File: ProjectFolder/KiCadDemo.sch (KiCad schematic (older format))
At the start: 9 parts, among them J1 1992, J2 TSW-103-07-T-S, J3 TSW-103-07-T-S, J4 TSW-103-07-T-S, J5 TSW-103-07-T-S

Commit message: Mostly finished PCB layout
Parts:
- added J6, J7: TSW-103-07-T-S, tsw-103-07-t-s:tsw-103-07-t-s, symbol TSW-103-07-T-S
- C2, C3: footprint Capacitors_SMD:C_1206 -> Capacitors_SMD:C_0805
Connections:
- net A1: now also J6.1, J7.1
- net A2: now also J6.2, J7.2
- net A3: now also J6.3, J7.3
- net AA: now also J1.26; no longer J1.32
- net AB: now also J1.33; no longer J1.36
- net CA: now also J1.35; no longer J1.38
- net CB: now also J1.38; no longer J1.40
- net S1C1: now also J3.1; no longer J2.1
- net S1C2: now also J3.2; no longer J2.2
- net S1C3: now also J3.3; no longer J2.3
- net S1_EN: now also J1.36; no longer J1.33
- net S2C1: now also J2.1; no longer J3.1
- net S2C2: now also J2.2; no longer J3.2
- net S2C3: now also J2.3; no longer J3.3
- net S2_EN: now also J1.40; no longer J1.35
- net S3_EN: now also J1.32; no longer J1.26
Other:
- moved on the sheet: J2, J3, J4, J5
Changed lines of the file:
@@
 L TSW-103-07-T-S J2
 U 1 1 55078EDE
-P 9200 3250
-F 0 "J2" H 9200 3500 60  0000 L CNN
-F 1 "TSW-103-07-T-S" H 9200 3000 60  0000 L CNN
-F 2 "tsw-103-07-t-s:tsw-103-07-t-s" H 9250 3250 60  0001 C CNN
-F 3 "" H 9250 3250 60  0000 C CNN
-F 4 "Samtec" H 9200 3250 60  0001 C CNN "Manufacturer"
-F 5 "TSW-103-07-T-S" H 9200 3250 60  0001 C CNN "Manufacturer Part Number"
-F 6 "Digi-Key" H 9200 3250 60  0001 C CNN "Supplier"
-F 7 "SAM1035-03-ND" H 9200 3250 60  0001 C CNN "Supplier Part Number"
-	1    9200 3250
-	1    0    0    -1
-$EndComp
-Text Label 8650 3150 0    60   ~ 0
+P 8250 3700
+F 0 "J2" H 8250 3950 60  0000 L CNN
+F 1 "TSW-103-07-T-S" H 8250 3450 60  0000 L CNN
+F 2 "tsw-103-07-t-s:tsw-103-07-t-s" H 8300 3700 60  0001 C CNN
+F 3 "" H 8300 3700 60  0000 C CNN
+F 4 "Samtec" H 8250 3700 60  0001 C CNN "Manufacturer"
+F 5 "TSW-103-07-T-S" H 8250 3700 60  0001 C CNN "Manufacturer Part Number"
+F 6 "Digi-Key" H 8250 3700 60  0001 C CNN "Supplier"
+F 7 "SAM1035-03-ND" H 8250 3700 60  0001 C CNN "Supplier Part Number"
+	1    8250 3700
+	1    0    0    -1
+$EndComp
+Text Label 7700 4350 0    60   ~ 0
 S1C1
 Wire Wire Line
-	8650 3150 9000 3150
-Text Label 8650 3250 0    60   ~ 0
+	7700 4350 8050 4350
+Text Label 7700 4450 0    60   ~ 0
 S1C2
 Wire Wire Line
-	8650 3250 9000 3250
-Text Label 8650 3350 0    60   ~ 0
+	7700 4450 8050 4450
+Text Label 7700 4550 0    60   ~ 0
 S1C3
 Wire Wire Line
-	8650 3350 9000 3350
-Text Label 8650 3900 0    60   ~ 0
+	7700 4550 8050 4550
+Text Label 7700 3600 0    60   ~ 0
 S2C1
 Wire Wire Line
-	8650 3900 9000 3900
-Text Label 8650 4000 0    60   ~ 0
+	7700 3600 8050 3600
+Text Label 7700 3700 0    60   ~ 0
 S2C2
 Wire Wire Line
-	8650 4000 9000 4000
-Text Label 8650 4100 0    60   ~ 0
+	7700 3700 8050 3700
+Text Label 7700 3800 0    60   ~ 0
 S2C3
 Wire Wire Line
-	8650 4100 9000 4100
-Text Label 8650 4650 0    60   ~ 0
+	7700 3800 8050 3800
+Text Label 7700 5100 0    60   ~ 0
 S3C1
 Wire Wire Line
-	8650 4650 9000 4650
-Text Label 8650 4750 0    60   ~ 0
+	7700 5100 8050 5100
+Text Label 7700 5200 0    60   ~ 0
 S3C2
 Wire Wire Line
-	8650 4750 9000 4750
-Text Label 8650 4850 0    60   ~ 0
+	7700 5200 8050 5200
+Text Label 7700 5300 0    60   ~ 0
 S3C3
 Wire Wire Line
-	8650 4850 9000 4850
-Text Label 8650 5400 0    60   ~ 0
+	7700 5300 8050 5300
+Text Label 9450 3600 0    60   ~ 0
 A1
 Wire Wire Line
-	8650 5400 9000 5400
-Text Label 8650 5500 0    60   ~ 0
+	9450 3600 9800 3600
+Text Label 9450 3700 0    60   ~ 0
 A2
 Wire Wire Line
-	8650 5500 9000 5500
-Text Label 8650 5600 0    60   ~ 0
+	9450 3700 9800 3700
+Text Label 9450 3800 0    60   ~ 0
 A3
 Wire Wire Line
-	8650 5600 9000 5600
+	9450 3800 9800 3800
+Text Label 2700 5150 2    60   ~ 0
+S2_EN
 Text Label 950  4950 0    60   ~ 0
-S2_EN
+CA
 Text Label 2700 5050 2    60   ~ 0
-CA
-Text Label 2700 5150 2    60   ~ 0
 CB
+Text Label 2700 4750 2    60   ~ 0
+S3_EN
 Text Label 2700 4450 2    60   ~ 0
-S3_EN
-Text Label 2700 4750 2    60   ~ 0
 AA
+Text Label 950  4850 0    60   ~ 0
+AB
 Text Label 2700 4950 2    60   ~ 0
-AB
-Text Label 950  4850 0    60   ~ 0
 S1_EN
 Wire Wire Line
@@
 F 0 "C2" H 2350 6500 50  0000 L CNN
 F 1 "0.1u" H 2350 6300 50  0000 L CNN
-F 2 "Capacitors_SMD:C_1206" H 2338 6250 30  0001 C CNN
+F 2 "Capacitors_SMD:C_0805" H 2338 6250 30  0001 C CNN
 F 3 "" H 2300 6400 60  0000 C CNN
 F 4 "16V" H 2450 6200 60  0001 C CNN "Voltage"
@@
 F 0 "C3" H 2800 6500 50  0000 L CNN
 F 1 "10u" H 2800 6300 50  0000 L CNN
-F 2 "Capacitors_SMD:C_1206" H 2788 6250 30  0001 C CNN
+F 2 "Capacitors_SMD:C_0805" H 2788 6250 30  0001 C CNN
 F 3 "" H 2750 6400 60  0000 C CNN
 F 4 "16V" H 2900 6200 60  0001 C CNN "Voltage"
@@
 L TSW-103-07-T-S J3
 U 1 1 550C2E47
-P 9200 4000
-F 0 "J3" H 9200 4250 60  0000 L CNN
-F 1 "TSW-103-07-T-S" H 9200 3750 60  0000 L CNN
-F 2 "tsw-103-07-t-s:tsw-103-07-t-s" H 9250 4000 60  0001 C CNN
-F 3 "" H 9250 4000 60  0000 C CNN
-F 4 "Samtec" H 9200 4000 60  0001 C CNN "Manufacturer"
-F 5 "TSW-103-07-T-S" H 9200 4000 60  0001 C CNN "Manufacturer Part Number"
-F 6 "Digi-Key" H 9200 4000 60  0001 C CNN "Supplier"
-F 7 "SAM1035-03-ND" H 9200 4000 60  0001 C CNN "Supplier Part Number"
-	1    9200 4000
+P 8250 4450
+F 0 "J3" H 8250 4700 60  0000 L CNN
+F 1 "TSW-103-07-T-S" H 8250 4200 60  0000 L CNN
+F 2 "tsw-103-07-t-s:tsw-103-07-t-s" H 8300 4450 60  0001 C CNN
+F 3 "" H 8300 4450 60  0000 C CNN
+F 4 "Samtec" H 8250 4450 60  0001 C CNN "Manufacturer"
+F 5 "TSW-103-07-T-S" H 8250 4450 60  0001 C CNN "Manufacturer Part Number"
+F 6 "Digi-Key" H 8250 4450 60  0001 C CNN "Supplier"
+F 7 "SAM1035-03-ND" H 8250 4450 60  0001 C CNN "Supplier Part Number"
+	1    8250 4450
 	1    0    0    -1
 $EndComp
@@
 L TSW-103-07-T-S J4
 U 1 1 550C2E90
-P 9200 4750
-F 0 "J4" H 9200 5000 60  0000 L CNN
-F 1 "TSW-103-07-T-S" H 9200 4500 60  0000 L CNN
-F 2 "tsw-103-07-t-s:tsw-103-07-t-s" H 9250 4750 60  0001 C CNN
-F 3 "" H 9250 4750 60  0000 C CNN
-F 4 "Samtec" H 9200 4750 60  0001 C CNN "Manufacturer"
-F 5 "TSW-103-07-T-S" H 9200 4750 60  0001 C CNN "Manufacturer Part Number"
-F 6 "Digi-Key" H 9200 4750 60  0001 C CNN "Supplier"
-F 7 "SAM1035-03-ND" H 9200 4750 60  0001 C CNN "Supplier Part Number"
-	1    9200 4750
+P 8250 5200
+F 0 "J4" H 8250 5450 60  0000 L CNN
+F 1 "TSW-103-07-T-S" H 8250 4950 60  0000 L CNN
+F 2 "tsw-103-07-t-s:tsw-103-07-t-s" H 8300 5200 60  0001 C CNN
+F 3 "" H 8300 5200 60  0000 C CNN
+F 4 "Samtec" H 8250 5200 60  0001 C CNN "Manufacturer"
+F 5 "TSW-103-07-T-S" H 8250 5200 60  0001 C CNN "Manufacturer Part Number"
+F 6 "Digi-Key" H 8250 5200 60  0001 C CNN "Supplier"
+F 7 "SAM1035-03-ND" H 8250 5200 60  0001 C CNN "Supplier Part Number"
+	1    8250 5200
 	1    0    0    -1
 $EndComp
@@
 L TSW-103-07-T-S J5
 U 1 1 550C2EDC
-P 9200 5500
-F 0 "J5" H 9200 5750 60  0000 L CNN
-F 1 "TSW-103-07-T-S" H 9200 5250 60  0000 L CNN
-F 2 "tsw-103-07-t-s:tsw-103-07-t-s" H 9250 5500 60  0001 C CNN
-F 3 "" H 9250 5500 60  0000 C CNN
-F 4 "Samtec" H 9200 5500 60  0001 C CNN "Manufacturer"
-F 5 "TSW-103-07-T-S" H 9200 5500 60  0001 C CNN "Manufacturer Part Number"
-F 6 "Digi-Key" H 9200 5500 60  0001 C CNN "Supplier"
-F 7 "SAM1035-03-ND" H 9200 5500 60  0001 C CNN "Supplier Part Number"
-	1    9200 5500
-	1    0    0    -1
-$EndComp
+P 10000 3700
+F 0 "J5" H 10000 3950 60  0000 L CNN
+F 1 "TSW-103-07-T-S" H 9400 3450 60  0000 L CNN
+F 2 "tsw-103-07-t-s:tsw-103-07-t-s" H 10050 3700 60  0001 C CNN
+F 3 "" H 10050 3700 60  0000 C CNN
+F 4 "Samtec" H 10000 3700 60  0001 C CNN "Manufacturer"
+F 5 "TSW-103-07-T-S" H 10000 3700 60  0001 C CNN "Manufacturer Part Number"
+F 6 "Digi-Key" H 10000 3700 60  0001 C CNN "Supplier"
+F 7 "SAM1035-03-ND" H 10000 3700 60  0001 C CNN "Supplier Part Number"
+	1    10000 3700
+	1    0    0    -1
+$EndComp
+Text Label 9450 4350 0    60   ~ 0
+A1
+Wire Wire Line
+	9450 4350 9800 4350
+Text Label 9450 4450 0    60   ~ 0
+A2
+Wire Wire Line
+	9450 4450 9800 4450
+Text Label 9450 4550 0    60   ~ 0
+A3
+Wire Wire Line
+	9450 4550 9800 4550
+$Comp
+L TSW-103-07-T-S J6
+U 1 1 550A6C58
+P 10000 4450
+F 0 "J6" H 10000 4700 60  0000 L CNN
+F 1 "TSW-103-07-T-S" H 9350 4200 60  0000 L CNN
+F 2 "tsw-103-07-t-s:tsw-103-07-t-s" H 10050 4450 60  0001 C CNN
+F 3 "" H 10050 4450 60  0000 C CNN
+F 4 "Samtec" H 10000 4450 60  0001 C CNN "Manufacturer"
+F 5 "TSW-103-07-T-S" H 10000 4450 60  0001 C CNN "Manufacturer Part Number"
+F 6 "Digi-Key" H 10000 4450 60  0001 C CNN "Supplier"
+F 7 "SAM1035-03-ND" H 10000 4450 60  0001 C CNN "Supplier Part Number"
+	1    10000 4450
+	1    0    0    -1
+$EndComp
+Text Label 9450 5100 0    60   ~ 0
+A1
+Wire Wire Line
+	9450 5100 9800 5100
+Text Label 9450 5200 0    60   ~ 0
+A2
+Wire Wire Line
+	9450 5200 9800 5200
+Text Label 9450 5300 0    60   ~ 0
+A3
+Wire Wire Line
+	9450 5300 9800 5300
+$Comp
+L TSW-103-07-T-S J7
+U 1 1 550A939F
+P 10000 5200
+F 0 "J7" H 10000 5450 60  0000 L CNN
+F 1 "TSW-103-07-T-S" H 9350 4950 60  0000 L CNN
+F 2 "tsw-103-07-t-s:tsw-103-07-t-s" H 10050 5200 60  0001 C CNN
+F 3 "" H 10050 5200 60  0000 C CNN
+F 4 "Samtec" H 10000 5200 60  0001 C CNN "Manufacturer"
+F 5 "TSW-103-07-T-S" H 10000 5200 60  0001 C CNN "Manufacturer Part Number"
+F 6 "Digi-Key" H 10000 5200 60  0001 C CNN "Supplier"
+F 7 "SAM1035-03-ND" H 10000 5200 60  0001 C CNN "Supplier Part Number"
+	1    10000 5200
+	1    0    0    -1
+$EndComp

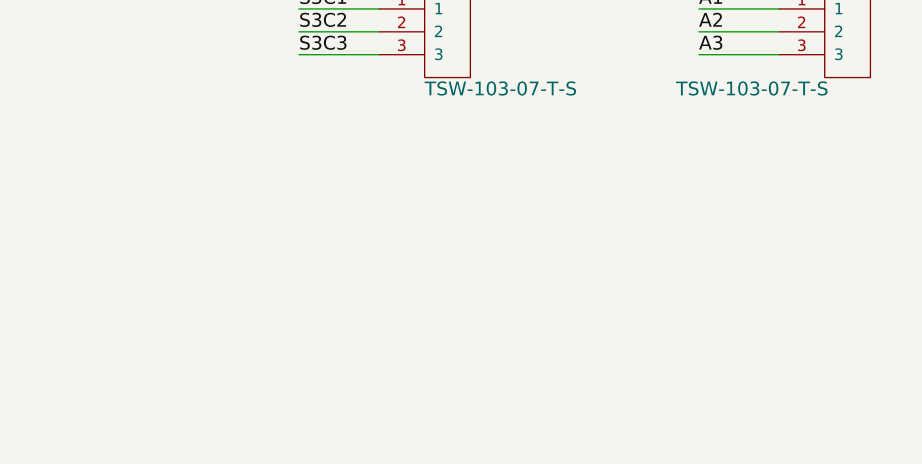
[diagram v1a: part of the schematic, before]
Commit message: Added mounting holes, fixed Raspberry Pi reference footprint mounting hole locations, and removed inaccurate mechanical drawing
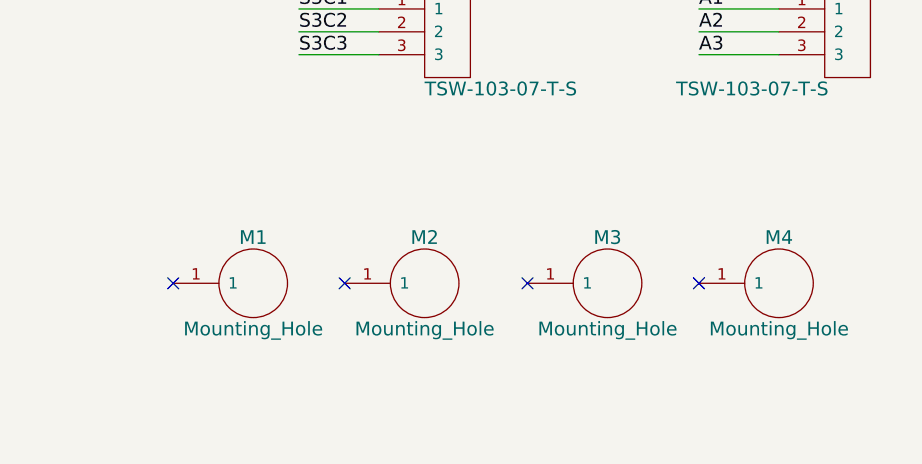
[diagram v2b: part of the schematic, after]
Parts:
- added M1, M2, M3, M4: Mounting_Hole, mounting_hole:mounting_hole_2.75mm_pth, symbol Mounting_Hole
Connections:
- no-connect marks 23 -> 27
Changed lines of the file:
@@
 LIBS:tsw-103-07-t-s
 LIBS:uln2003adr
+LIBS:mounting_hole
 LIBS:KiCadDemo-cache
 EELAYER 25 0
@@
 Sheet 1 2
 Title "Raspberry Pi 3x3x3 LED Cube Shield, Main PCB"
-Date "Tuesday, March 17, 2015"
+Date "Thursday, March 19, 2015"
 Rev "-"
 Comp ""
@@
 	1    0    0    -1
 $EndComp
+$Comp
+L Mounting_Hole M4
+U 1 1 550B8F13
+P 9800 6300
+F 0 "M4" H 9800 6500 60  0000 C CNN
+F 1 "Mounting_Hole" H 9800 6100 60  0000 C CNN
+F 2 "mounting_hole:mounting_hole_2.75mm_pth" H 9800 6300 60  0001 C CNN
+F 3 "" H 9800 6300 60  0000 C CNN
+	1    9800 6300
+	1    0    0    -1
+$EndComp
+$Comp
+L Mounting_Hole M3
+U 1 1 550B8ED3
+P 9050 6300
+F 0 "M3" H 9050 6500 60  0000 C CNN
+F 1 "Mounting_Hole" H 9050 6100 60  0000 C CNN
+F 2 "mounting_hole:mounting_hole_2.75mm_pth" H 9050 6300 60  0001 C CNN
+F 3 "" H 9050 6300 60  0000 C CNN
+	1    9050 6300
+	1    0    0    -1
+$EndComp
+$Comp
+L Mounting_Hole M2
+U 1 1 550B8E7F
+P 8250 6300
+F 0 "M2" H 8250 6500 60  0000 C CNN
+F 1 "Mounting_Hole" H 8250 6100 60  0000 C CNN
+F 2 "mounting_hole:mounting_hole_2.75mm_pth" H 8250 6300 60  0001 C CNN
+F 3 "" H 8250 6300 60  0000 C CNN
+	1    8250 6300
+	1    0    0    -1
+$EndComp
+$Comp
+L Mounting_Hole M1
+U 1 1 550B74AD
+P 7500 6300
+F 0 "M1" H 7500 6500 60  0000 C CNN
+F 1 "Mounting_Hole" H 7500 6100 60  0000 C CNN
+F 2 "mounting_hole:mounting_hole_2.75mm_pth" H 7500 6300 60  0001 C CNN
+F 3 "" H 7500 6300 60  0000 C CNN
+	1    7500 6300
+	1    0    0    -1
+$EndComp
+NoConn ~ 7150 6300
+NoConn ~ 7900 6300
+NoConn ~ 8700 6300
+NoConn ~ 9450 6300
 $EndSCHEMATC

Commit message: branch to store exercise project, remove mounting holes including libraries
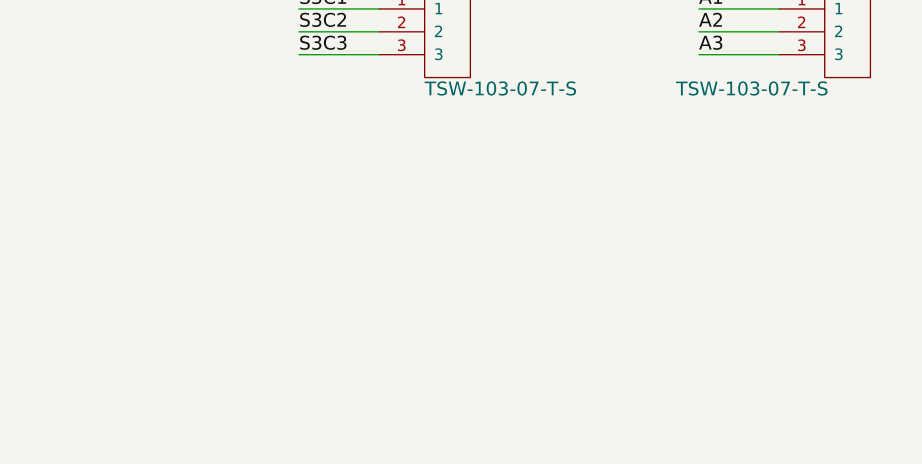
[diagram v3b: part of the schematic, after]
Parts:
- removed M1, M2, M3, M4: Mounting_Hole, mounting_hole:mounting_hole_2.75mm_pth, symbol Mounting_Hole
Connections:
- no-connect marks 27 -> 23
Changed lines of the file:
@@
 LIBS:tsw-103-07-t-s
 LIBS:uln2003adr
-LIBS:mounting_hole
 LIBS:KiCadDemo-cache
 EELAYER 25 0
@@
 	1    0    0    -1
 $EndComp
-$Comp
-L Mounting_Hole M4
-U 1 1 550B8F13
-P 9800 6300
-F 0 "M4" H 9800 6500 60  0000 C CNN
-F 1 "Mounting_Hole" H 9800 6100 60  0000 C CNN
-F 2 "mounting_hole:mounting_hole_2.75mm_pth" H 9800 6300 60  0001 C CNN
-F 3 "" H 9800 6300 60  0000 C CNN
-	1    9800 6300
-	1    0    0    -1
-$EndComp
-$Comp
-L Mounting_Hole M3
-U 1 1 550B8ED3
-P 9050 6300
-F 0 "M3" H 9050 6500 60  0000 C CNN
-F 1 "Mounting_Hole" H 9050 6100 60  0000 C CNN
-F 2 "mounting_hole:mounting_hole_2.75mm_pth" H 9050 6300 60  0001 C CNN
-F 3 "" H 9050 6300 60  0000 C CNN
-	1    9050 6300
-	1    0    0    -1
-$EndComp
-$Comp
-L Mounting_Hole M2
-U 1 1 550B8E7F
-P 8250 6300
-F 0 "M2" H 8250 6500 60  0000 C CNN
-F 1 "Mounting_Hole" H 8250 6100 60  0000 C CNN
-F 2 "mounting_hole:mounting_hole_2.75mm_pth" H 8250 6300 60  0001 C CNN
-F 3 "" H 8250 6300 60  0000 C CNN
-	1    8250 6300
-	1    0    0    -1
-$EndComp
-$Comp
-L Mounting_Hole M1
-U 1 1 550B74AD
-P 7500 6300
-F 0 "M1" H 7500 6500 60  0000 C CNN
-F 1 "Mounting_Hole" H 7500 6100 60  0000 C CNN
-F 2 "mounting_hole:mounting_hole_2.75mm_pth" H 7500 6300 60  0001 C CNN
-F 3 "" H 7500 6300 60  0000 C CNN
-	1    7500 6300
-	1    0    0    -1
-$EndComp
-NoConn ~ 7150 6300
-NoConn ~ 7900 6300
-NoConn ~ 8700 6300
-NoConn ~ 9450 6300
 $EndSCHEMATC
